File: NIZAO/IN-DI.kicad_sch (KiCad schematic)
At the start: 6 parts, among them U5 AT3H4B-CUH-S

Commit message: actualizado
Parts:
- removed U5: AT3H4B-CUH-S, AOTE AT3H4B-CuH-S:SSOP-4_L2.7-W4.6-P1.27-LS7.0-TL, symbol easyeda2kicad:AT3H4B-CUH-S
- added U19: AT3H4B-CUH-S, EasyEDA:SSOP-4_L2.7-W4.6-P1.27-LS7.0-TL, symbol EasyEDA:AT3H4B-CUH-S
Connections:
- net COM: now also U19.2 (CAT/AN)
- net GND: now also U19.3 (EM)
- net OUT: now also U19.4 (COL)
- net at C17.1, R17.2, R18.2: now also U19.1 (AN/CAT)
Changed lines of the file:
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@@
+	)
+	(symbol
+		(lib_id "EasyEDA:AT3H4B-CUH-S")
+		(at 142.24 97.79 0)
+		(unit 1)
+		(exclude_from_sim no)
+		(in_bom yes)
+		(on_board yes)
+		(dnp no)
+		(fields_autoplaced yes)
+		(property "Reference" "U19"
+			(at 157.48 92.71 0)
+			(effects
+				(font
+					(size 1.27 1.27)
+				)
+			)
+		)
+		(property "Value" "AT3H4B-CUH-S"
+			(at 157.48 95.25 0)
+			(effects
+				(font
+					(size 1.27 1.27)
+				)
+			)
+		)
+		(property "Footprint" "EasyEDA:SSOP-4_L2.7-W4.6-P1.27-LS7.0-TL"
+			(at 142.24 118.11 0)
+			(effects
+				(font
+					(size 1.27 1.27)
+				)
+				(hide yes)
+			)
+		)
+		(property "Datasheet" ""
+			(at 142.24 97.79 0)
+			(effects
+				(font
+					(size 1.27 1.27)
+				)
+				(hide yes)
+			)
+		)
+		(property "Description" ""
+			(at 142.24 97.79 0)
+			(effects
+				(font
+					(size 1.27 1.27)
+				)
+				(hide yes)
+			)
+		)
+		(property "LCSC Part" "C20612635"
+			(at 142.24 120.65 0)
+			(effects
+				(font
+					(size 1.27 1.27)
+				)
+				(hide yes)
+			)
+		)
+		(pin "4"
+		)
+		(pin "2"
+		)
+		(pin "1"
+		)
+		(pin "3"
+		)
+		(instances
+			(project ""
+				(path "/02cf9799-02a7-405e-973c-e989305c6b7d/a351403f-f255-4be6-b82d-8c5a977ae079/15471b0f-f04d-42c9-8427-33bf677c8fd1"
+					(reference "U23")
+					(unit 1)
+				)
+				(path "/02cf9799-02a7-405e-973c-e989305c6b7d/a351403f-f255-4be6-b82d-8c5a977ae079/42636844-d0a6-4ffb-afef-be78e472d752"
+					(reference "U24")
+					(unit 1)
+				)
+				(path "/02cf9799-02a7-405e-973c-e989305c6b7d/a351403f-f255-4be6-b82d-8c5a977ae079/7cb4a06e-4fbf-4d1a-a1d1-1bcc1b82ebea"
+					(reference "U22")
+					(unit 1)
+				)
+				(path "/02cf9799-02a7-405e-973c-e989305c6b7d/a351403f-f255-4be6-b82d-8c5a977ae079/e33c5eef-b54a-45c3-ba67-23bd220a82f1"
+					(reference "U21")
+					(unit 1)
+				)
+				(path "/02cf9799-02a7-405e-973c-e989305c6b7d/a351403f-f255-4be6-b82d-8c5a977ae079/f009e054-4e5b-4f71-b730-946c3e9efa14"
+					(reference "U19")
+					(unit 1)
+				)
+				(path "/02cf9799-02a7-405e-973c-e989305c6b7d/a351403f-f255-4be6-b82d-8c5a977ae079/f9d16392-2495-49bb-b65f-6cb01a6522f8"
+					(reference "U20")
+					(unit 1)
+				)
+			)
+		)
 	)
 	(symbol
@@
 					(unit 1)
 				)
-			)
-		)
-	)
-	(symbol
-		(lib_id "easyeda2kicad:AT3H4B-CUH-S")
-		(at 157.48 105.41 0)
-		(unit 1)
-		(exclude_from_sim no)
-		(in_bom yes)
-		(on_board yes)
-		(dnp no)
-		(property "Reference" "U5"
-			(at 157.48 92.71 0)
-			(effects
-				(font
-					(size 1.27 1.27)
-				)
-			)
-		)
-		(property "Value" "AT3H4B-CUH-S"
-			(at 157.48 95.25 0)
-			(effects
-				(font
-					(size 1.27 1.27)
-				)
-			)
-		)
-		(property "Footprint" "AOTE AT3H4B-CuH-S:SSOP-4_L2.7-W4.6-P1.27-LS7.0-TL"
-			(at 157.48 118.11 0)
-			(effects
-				(font
-					(size 1.27 1.27)
-				)
-				(hide yes)
-			)
-		)
-		(property "Datasheet" ""
-			(at 157.48 105.41 0)
-			(effects
-				(font
-					(size 1.27 1.27)
-				)
-				(hide yes)
-			)
-		)
-		(property "Description" ""
-			(at 157.48 105.41 0)
-			(effects
-				(font
-					(size 1.27 1.27)
-				)
-				(hide yes)
-			)
-		)
-		(property "LCSC Part" "C20612635"
-			(at 157.48 120.65 0)
-			(effects
-				(font
-					(size 1.27 1.27)
-				)
-				(hide yes)
-			)
-		)
-		(pin "1"
-		)
-		(pin "2"
-		)
-		(pin "3"
-		)
-		(pin "4"
-		)
-		(instances
-			(project "NIZAO"
-				(path "/02cf9799-02a7-405e-973c-e989305c6b7d/a351403f-f255-4be6-b82d-8c5a977ae079/15471b0f-f04d-42c9-8427-33bf677c8fd1"
-					(reference "U9")
-					(unit 1)
-				)
-				(path "/02cf9799-02a7-405e-973c-e989305c6b7d/a351403f-f255-4be6-b82d-8c5a977ae079/42636844-d0a6-4ffb-afef-be78e472d752"
-					(reference "U10")
-					(unit 1)
-				)
-				(path "/02cf9799-02a7-405e-973c-e989305c6b7d/a351403f-f255-4be6-b82d-8c5a977ae079/7cb4a06e-4fbf-4d1a-a1d1-1bcc1b82ebea"
-					(reference "U8")
-					(unit 1)
-				)
-				(path "/02cf9799-02a7-405e-973c-e989305c6b7d/a351403f-f255-4be6-b82d-8c5a977ae079/e33c5eef-b54a-45c3-ba67-23bd220a82f1"
-					(reference "U7")
-					(unit 1)
-				)
-				(path "/02cf9799-02a7-405e-973c-e989305c6b7d/a351403f-f255-4be6-b82d-8c5a977ae079/f009e054-4e5b-4f71-b730-946c3e9efa14"
-					(reference "U5")
-					(unit 1)
-				)
-				(path "/02cf9799-02a7-405e-973c-e989305c6b7d/a351403f-f255-4be6-b82d-8c5a977ae079/f9d16392-2495-49bb-b65f-6cb01a6522f8"
-					(reference "U6")
-					(unit 1)
-				)

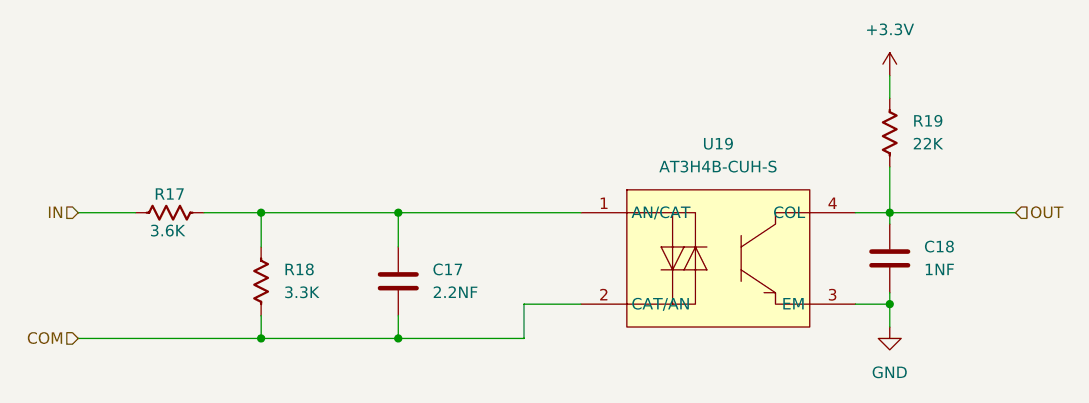
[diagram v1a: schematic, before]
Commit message: Colocandos los 3d de los componetes en la placa NIZAO
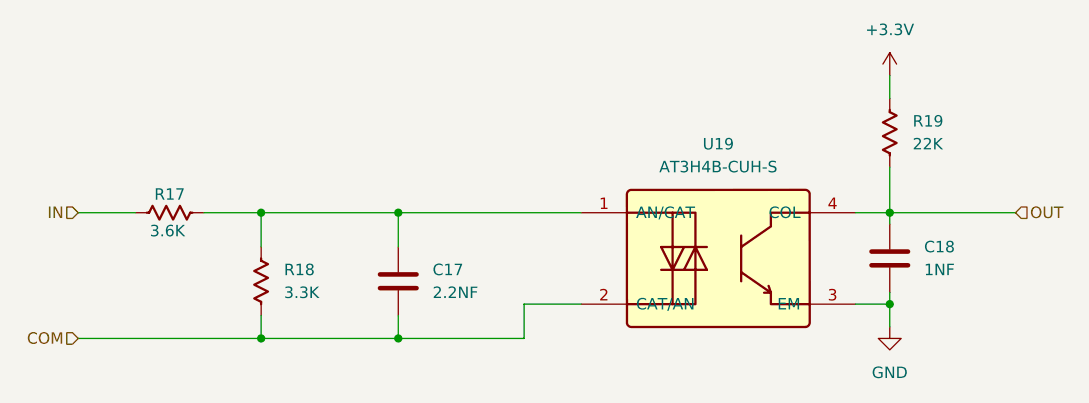
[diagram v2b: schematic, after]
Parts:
- U19: footprint EasyEDA:SSOP-4_L2.7-W4.6-P1.27-LS7.0-TL -> JLCImport:AT3H4B-CUH-S; symbol EasyEDA:AT3H4B-CUH-S -> JLCImport:AT3H4B-CUH-S; LCSC (none) -> C20612635; Manufacturer (none) -> AOTE; Manufacturer Part (none) -> AT3H4B-CuH-S
